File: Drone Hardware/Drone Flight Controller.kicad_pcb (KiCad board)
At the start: 2 copper layers, 51 parts, among them J1 USB_B_Micro, J10 UART6_RX, J11 SDA_PAD, J12 PPM_IN, J13 UART3_TX, J14 UART3_RX, J15 Pad, J2 S4, J3 S1, J4 UART1_TX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

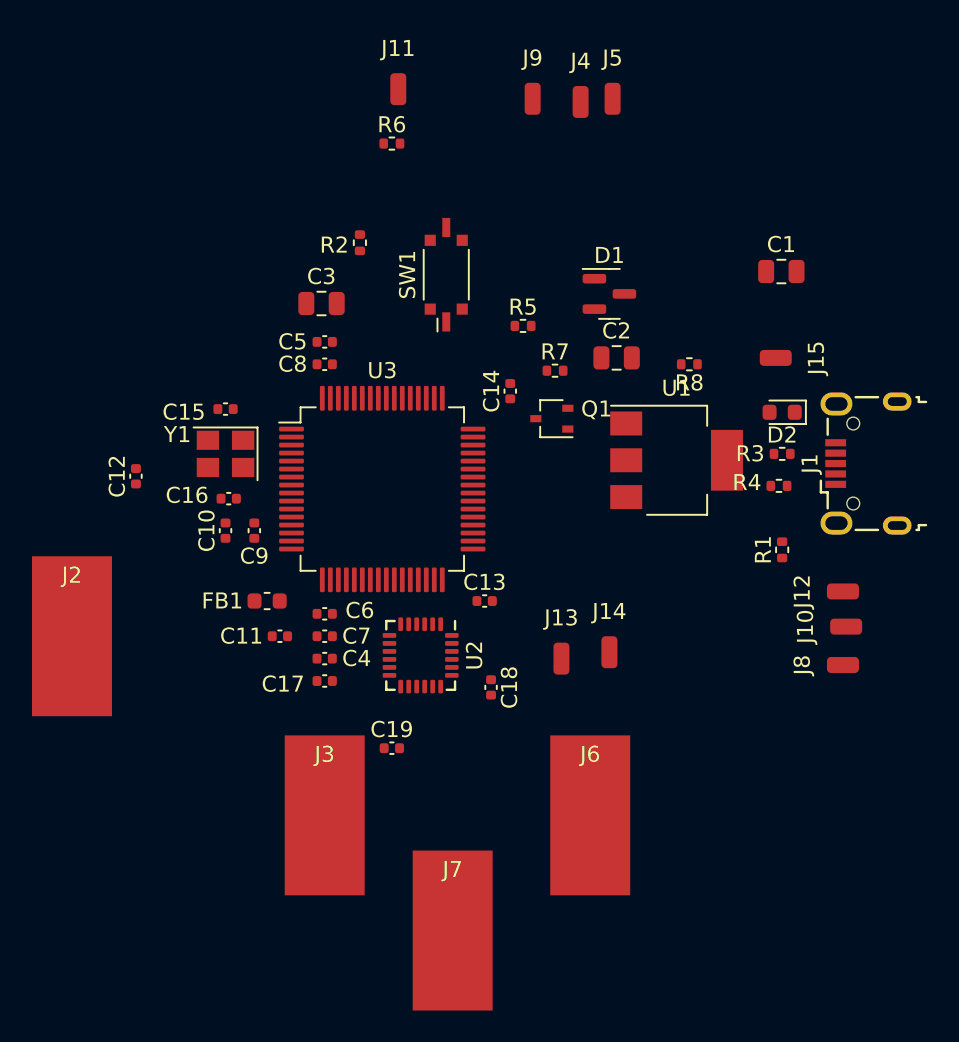
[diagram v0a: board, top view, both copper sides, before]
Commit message: Wired the decoupling capacitors, crystal and USB
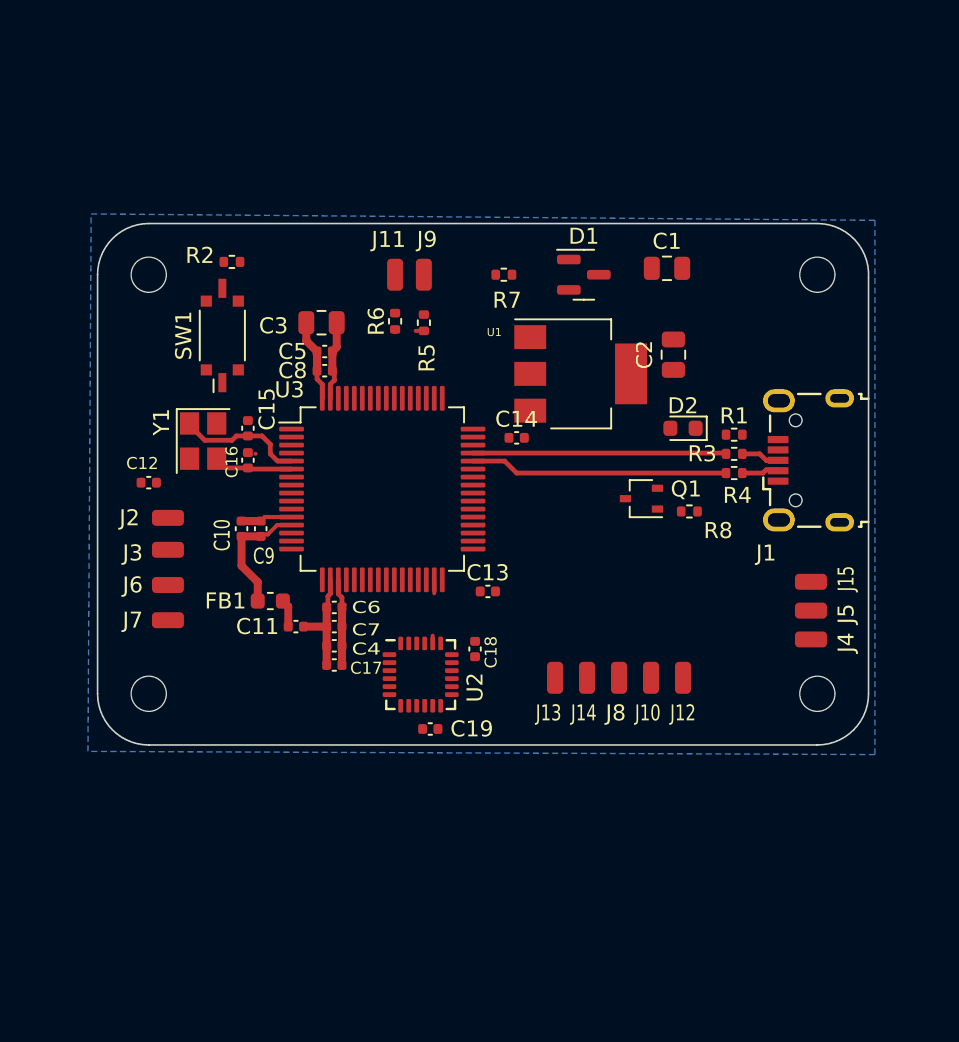
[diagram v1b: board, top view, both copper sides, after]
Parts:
- added H1: MountingHole, MountingHole:MountingHole_2.2mm_M2, F.Cu at (84.0, 76.6)
- added H2: MountingHole, MountingHole:MountingHole_2.2mm_M2, F.Cu at (42.2, 76.6)
- added H3: MountingHole, MountingHole:MountingHole_2.2mm_M2, F.Cu at (42.2, 102.8)
- added H4: MountingHole, MountingHole:MountingHole_2.2mm_M2, F.Cu at (84.0, 102.8)
- J2: value S4 -> S1; footprint Connector_Wire:SolderWirePad_1x01_SMD_5x10mm -> Connector_Wire:SolderWirePad_1x01_SMD_1x2mm
- J3: value S1 -> S4; footprint Connector_Wire:SolderWirePad_1x01_SMD_5x10mm -> Connector_Wire:SolderWirePad_1x01_SMD_1x2mm
- J6: value S2 -> S3; footprint Connector_Wire:SolderWirePad_1x01_SMD_5x10mm -> Connector_Wire:SolderWirePad_1x01_SMD_1x2mm
- J7: value S3 -> S2; footprint Connector_Wire:SolderWirePad_1x01_SMD_5x10mm -> Connector_Wire:SolderWirePad_1x01_SMD_1x2mm
- moved J4 36.6 mm to (83.6, 99.4), turned to -90 degrees
- moved J5 34.3 mm to (83.6, 97.6), turned to -90 degrees
- moved J6 30.1 mm to (43.4, 96.0), turned to -90 degrees
- moved J7 26.3 mm to (43.4, 98.2), turned to -90 degrees
- moved J3 19.3 mm to (43.4, 93.8), turned to -90 degrees
- moved SW1 14.5 mm to (46.8, 80.4)
- moved J15 14.2 mm to (83.6, 95.8)
- moved J8 14.0 mm to (71.6, 101.8), turned to 0 degrees
- moved J9 12.9 mm to (59.4, 76.6)
- moved J10 12.6 mm to (73.6, 101.8), turned to 0 degrees
- moved J11 11.6 mm to (57.6, 76.6)
- moved J12 11.4 mm to (75.6, 101.8), turned to 0 degrees
- moved R6 11.1 mm to (57.6, 79.5), turned to 90 degrees
- moved J2 9.53 mm to (43.4, 91.8), turned to -90 degrees
- moved R8 9.20 mm to (76.0, 91.4)
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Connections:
- J2 pad 1: /S4 -> /S1
- J3 pad 1: /S1 -> /S4
- J6 pad 1: /S2 -> /S3
- J7 pad 1: /S3 -> /S2
- U3 pad 10: unconnected-(U3-Pad10) -> /S3
- U3 pad 11: unconnected-(U3-Pad11) -> /S2
- U3 pad 16: /S4 -> unconnected-(U3-Pad16)
- U3 pad 17: /S1 -> unconnected-(U3-Pad17)
- U3 pad 26: /S2 -> unconnected-(U3-Pad26)
- U3 pad 27: /S3 -> unconnected-(U3-Pad27)
- U3 pad 8: unconnected-(U3-Pad8) -> /S1
- U3 pad 9: unconnected-(U3-Pad9) -> /S4
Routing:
- net /USB_OTG_FS_DM: track 0.00 -> 16.1 mm
- net /USB_OTG_FS_DP: track 0.00 -> 15.8 mm
- net GND: track 0.00 -> 15.2 mm
- net +3.3V: track 0.00 -> 13.6 mm
- net +3.3VA: track 0.00 -> 8.09 mm
- net /RCC_OSC_IN: track 0.00 -> 7.98 mm
- net /RCC_OSC_OUT: track 0.00 -> 5.78 mm
- net Net-(J1-Pad3): track 0.00 -> 2.40 mm
- net Net-(J1-Pad2): track 0.00 -> 2.34 mm
- net Net-(C13-Pad1): track 0.00 -> 0.84 mm
- net /PPM_IN: track 0.00 -> 0.80 mm
- net /SCL_PAD: track 0.00 -> 0.51 mm
- added copper zone on B.Cu, net GND
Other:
- board outline added: 48.2 x 32.6 mm

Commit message: Reconfigured linux repository and finished version 1.0 of the flight controller.
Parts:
- removed J15: Pad, Connector_Wire:SolderWirePad_1x01_SMD_1x2mm
- added ?: , , F.Cu at (79.6, 79.2)
- added ?: , , F.Cu at (79.6, 81.2)
- moved R7 15.7 mm to (70.2, 91.2), turned to -90 degrees
- moved C12 10.7 mm to (51.4, 84.2)
- moved D2 10.6 mm to (76.6, 75.6), turned to 90 degrees
- moved R1 8.99 mm to (75.6, 78.2), turned to 180 degrees
- moved C1 8.30 mm to (72.4, 84.2)
- moved D1 8.24 mm to (68.6, 84.8), turned to 90 degrees
- moved J4 7.40 mm to (76.6, 101.8), turned to 180 degrees
- moved J5 6.53 mm to (78.6, 101.8), turned to 180 degrees
- moved C2 5.83 mm to (74.4, 75.8)
- moved U1 4.80 mm to (69.2, 78.0), turned to 90 degrees
- moved C19 4.24 mm to (56.8, 102.0), turned to -90 degrees
- moved C18 2.53 mm to (63.4, 102.4)
- moved C13 1.17 mm to (62.4, 95.8)
- moved J10 1.00 mm to (72.6, 101.8)
- moved J12 1.00 mm to (74.6, 101.8)
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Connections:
- C1 pad 1: Net-(C1-Pad1) -> +5V
- D1 pad 1: +5V -> VDD
- D1 pad 3: Net-(C1-Pad1) -> +5V
- J5 pad 1: UART1_RX -> Net-(J5-Pad1)
- Q1 pad 3: UART1_RX -> UART1_RX_OUT
- R7 pad 1: UART1_RX -> UART1_RX_OUT
- R8 pad 1: Net-(J15-Pad1) -> Net-(J5-Pad1)
- U1 pad 3: Net-(C1-Pad1) -> +5V
- U3 pad 43: UART1_RX -> UART1_RX_OUT
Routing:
- net +3.3V: track 13.6 -> 104.2 mm, vias 0 -> 6
- net GND: track 15.2 -> 62.5 mm, vias 0 -> 17
- net SPI1_SCLK: track 0.00 -> 24.3 mm
- net VBUS: track 0.00 -> 22.5 mm
- net /UART1_TX: track 0.00 -> 19.3 mm
- net +5V: track 0.00 -> 18.8 mm, vias 0 -> 2
- net VDD: track 0.00 -> 18.2 mm, vias 0 -> 2
- net /PPM_IN: track 0.80 -> 17.1 mm
- net /UART6_RX: track 0.00 -> 15.4 mm
- net /BOOT0: track 0.00 -> 14.7 mm
- net GYRO_INT: track 0.00 -> 13.8 mm, vias 0 -> 2
- net /UART6_TX: track 0.20 -> 13.9 mm
- net /UART3_RX: track 0.00 -> 12.9 mm
- net /S2: track 0.00 -> 12.3 mm
- net Net-(J5-Pad1): track 0.00 -> 11.3 mm
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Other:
- board text added: "Designed by Andres Cruz Brogurt Inc."
